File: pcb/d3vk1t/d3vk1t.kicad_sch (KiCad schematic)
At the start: 0 parts

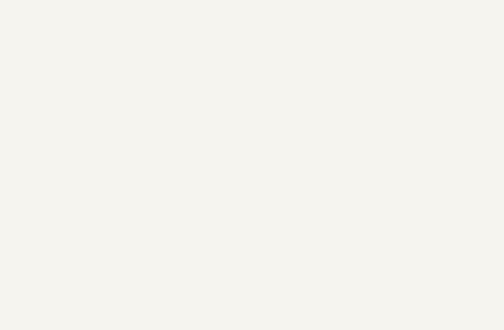
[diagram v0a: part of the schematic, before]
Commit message: [doc: update mcu pinout, pcb: update board shape]
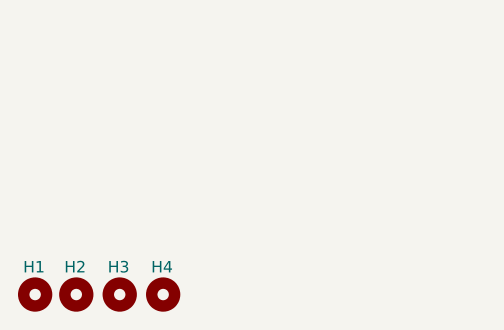
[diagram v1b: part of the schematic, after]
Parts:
- added H1, H2, H3, H4: MountingHole, MountingHole:MountingHole_3.2mm_M3_Pad_Via, symbol Mechanical:MountingHole
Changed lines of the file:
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@@
 (kicad_sch (version 20230121) (generator eeschema)
   (paper "A4")
+  (symbol (lib_id "Mechanical:MountingHole") (at 61.214 178.562 0) (unit 1)
+    (in_bom yes) (on_board yes) (dnp no)
+    (property "Reference" "H4" (at 59.8799 175.5177 0)
+      (effects (font (size 1.27 1.27)) (justify left))
+    )
+    (property "Value" "MountingHole" (at 64.008 180.467 0)
+      (effects (font (size 1.27 1.27)) (justify left) hide)
+    )
+    (property "Footprint" "MountingHole:MountingHole_3.2mm_M3_Pad_Via" (at 61.214 178.562 0)
+      (effects (font (size 1.27 1.27)) hide)
+    )
+    (property "Datasheet" "~" (at 61.214 178.562 0)
+      (effects (font (size 1.27 1.27)) hide)
+    )
+    (instances
+      (project "d3vk1t"
+        (path "/4ea523ae-7c45-478e-a9cc-6f4833d1a9d5"
+          (reference "H4") (unit 1)
+        )
+      )
+    )
+  )
+  (symbol (lib_id "Mechanical:MountingHole") (at 51.562 178.562 0) (unit 1)
+    (in_bom yes) (on_board yes) (dnp no)
+    (property "Reference" "H2" (at 50.2279 175.5177 0)
+      (effects (font (size 1.27 1.27)) (justify left))
+    )
+    (property "Value" "MountingHole" (at 54.356 180.467 0)
+      (effects (font (size 1.27 1.27)) (justify left) hide)
+    )
+    (property "Footprint" "MountingHole:MountingHole_3.2mm_M3_Pad_Via" (at 51.562 178.562 0)
+      (effects (font (size 1.27 1.27)) hide)
+    )
+    (property "Datasheet" "~" (at 51.562 178.562 0)
+      (effects (font (size 1.27 1.27)) hide)
+    )
+    (instances
+      (project "d3vk1t"
+        (path "/4ea523ae-7c45-478e-a9cc-6f4833d1a9d5"
+          (reference "H2") (unit 1)
+        )
+      )
+    )
+  )
+  (symbol (lib_id "Mechanical:MountingHole") (at 56.388 178.562 0) (unit 1)
+    (in_bom yes) (on_board yes) (dnp no)
+    (property "Reference" "H3" (at 55.0539 175.5177 0)
+      (effects (font (size 1.27 1.27)) (justify left))
+    )
+    (property "Value" "MountingHole" (at 59.182 180.467 0)
+      (effects (font (size 1.27 1.27)) (justify left) hide)
+    )
+    (property "Footprint" "MountingHole:MountingHole_3.2mm_M3_Pad_Via" (at 56.388 178.562 0)
+      (effects (font (size 1.27 1.27)) hide)
+    )
+    (property "Datasheet" "~" (at 56.388 178.562 0)
+      (effects (font (size 1.27 1.27)) hide)
+    )
+    (instances
+      (project "d3vk1t"
+        (path "/4ea523ae-7c45-478e-a9cc-6f4833d1a9d5"
+          (reference "H3") (unit 1)
+        )
+      )
+    )
+  )
+  (symbol (lib_id "Mechanical:MountingHole") (at 46.99 178.562 0) (unit 1)
+    (in_bom yes) (on_board yes) (dnp no)
+    (property "Reference" "H1" (at 45.6559 175.5177 0)
+      (effects (font (size 1.27 1.27)) (justify left))
+    )
+    (property "Value" "MountingHole" (at 49.784 180.467 0)
+      (effects (font (size 1.27 1.27)) (justify left) hide)
+    )
+    (property "Footprint" "MountingHole:MountingHole_3.2mm_M3_Pad_Via" (at 46.99 178.562 0)
+      (effects (font (size 1.27 1.27)) hide)
+    )
+    (property "Datasheet" "~" (at 46.99 178.562 0)
+      (effects (font (size 1.27 1.27)) hide)
+    )
+    (instances
+      (project "d3vk1t"
+        (path "/4ea523ae-7c45-478e-a9cc-6f4833d1a9d5"
+          (reference "H1") (unit 1)
+        )
+      )
+    )
+  )
   (sheet (at 85.852 71.882) (size 22.352 13.97) (fields_autoplaced)
     (stroke (width 0.1524) (type solid))

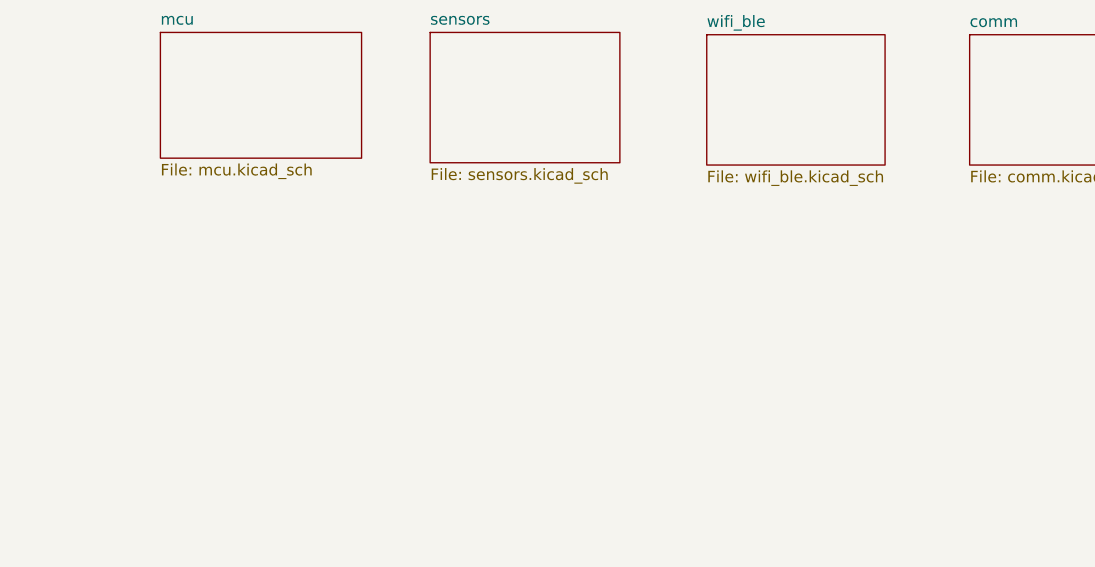
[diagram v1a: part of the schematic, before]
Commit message: doc: added f4 hw dev doc
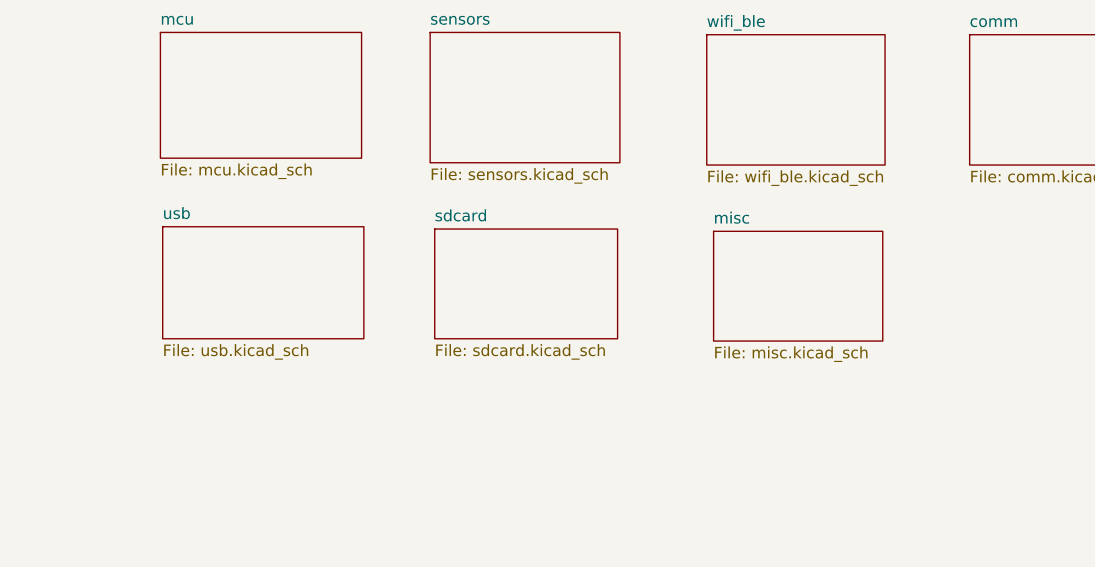
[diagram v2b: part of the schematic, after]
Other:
- added sheet misc (misc.kicad_sch)
- added sheet sdcard (sdcard.kicad_sch)
- added sheet usb (usb.kicad_sch)
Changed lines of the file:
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@@
+    )
+  )
+  (sheet (at 116.332 93.726) (size 20.32 12.192) (fields_autoplaced)
+    (stroke (width 0.1524) (type solid))
+    (fill (color 0 0 0 0.0000))
+    (property "Sheetname" "sdcard" (at 116.332 93.0144 0)
+      (effects (font (size 1.27 1.27)) (justify left bottom))
+    )
+    (property "Sheetfile" "sdcard.kicad_sch" (at 116.332 106.5026 0)
+      (effects (font (size 1.27 1.27)) (justify left top))
+    )
+    (instances
+      (project "d3vk1t"
+        (path "/4ea523ae-7c45-478e-a9cc-6f4833d1a9d5" (page "7"))
+      )
     )
   )
@@
     )
   )
+  (sheet (at 147.32 93.98) (size 18.796 12.192) (fields_autoplaced)
+    (stroke (width 0.1524) (type solid))
+    (fill (color 0 0 0 0.0000))
+    (property "Sheetname" "misc" (at 147.32 93.2684 0)
+      (effects (font (size 1.27 1.27)) (justify left bottom))
+    )
+    (property "Sheetfile" "misc.kicad_sch" (at 147.32 106.7566 0)
+      (effects (font (size 1.27 1.27)) (justify left top))
+    )
+    (instances
+      (project "d3vk1t"
+        (path "/4ea523ae-7c45-478e-a9cc-6f4833d1a9d5" (page "8"))
+      )
+    )
+  )
   (sheet (at 175.768 72.136) (size 22.352 14.478) (fields_autoplaced)
     (stroke (width 0.1524) (type solid))
@@
       )
     )
+  )
+  (sheet (at 86.106 93.472) (size 22.352 12.446) (fields_autoplaced)
+    (stroke (width 0.1524) (type solid))
+    (fill (color 0 0 0 0.0000))
+    (property "Sheetname" "usb" (at 86.106 92.7604 0)
+      (effects (font (size 1.27 1.27)) (justify left bottom))
+    )
+    (property "Sheetfile" "usb.kicad_sch" (at 86.106 106.5026 0)
+      (effects (font (size 1.27 1.27)) (justify left top))
+    )
+    (instances
+      (project "d3vk1t"
+        (path "/4ea523ae-7c45-478e-a9cc-6f4833d1a9d5" (page "6"))
+      )
+    )

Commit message: [update all schematics sheets]
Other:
- added sheet display (display.kicad_sch)
- added sheet memories (memories.kicad_sch)
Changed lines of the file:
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@@
     )
   )
-  (sheet (at 85.852 71.882) (size 22.352 13.97) (fields_autoplaced)
+  (sheet (at 132.08 76.2) (size 20.32 33.02)
     (stroke (width 0.1524) (type solid))
     (fill (color 0 0 0 0.0000))
-    (property "Sheetname" "mcu" (at 85.852 71.1704 0)
+    (property "Sheetname" "mcu" (at 132.08 75.4884 0)
       (effects (font (size 1.27 1.27)) (justify left bottom))
     )
-    (property "Sheetfile" "mcu.kicad_sch" (at 85.852 86.4366 0)
+    (property "Sheetfile" "mcu.kicad_sch" (at 132.08 109.22 0)
       (effects (font (size 1.27 1.27)) (justify left top))
     )
@@
     )
   )
-  (sheet (at 146.558 72.136) (size 19.812 14.478) (fields_autoplaced)
+  (sheet (at 167.64 78.74) (size 20.32 12.7) (fields_autoplaced)
     (stroke (width 0.1524) (type solid))
     (fill (color 0 0 0 0.0000))
-    (property "Sheetname" "wifi_ble" (at 146.558 71.4244 0)
+    (property "Sheetname" "wifi_ble" (at 167.64 78.0284 0)
       (effects (font (size 1.27 1.27)) (justify left bottom))
     )
-    (property "Sheetfile" "wifi_ble.kicad_sch" (at 146.558 87.1986 0)
+    (property "Sheetfile" "wifi_ble.kicad_sch" (at 167.64 92.0246 0)
       (effects (font (size 1.27 1.27)) (justify left top))
     )
@@
     )
   )
-  (sheet (at 116.332 93.726) (size 20.32 12.192) (fields_autoplaced)
+  (sheet (at 167.64 116.84) (size 20.32 12.7) (fields_autoplaced)
     (stroke (width 0.1524) (type solid))
     (fill (color 0 0 0 0.0000))
-    (property "Sheetname" "sdcard" (at 116.332 93.0144 0)
+    (property "Sheetname" "display" (at 167.64 116.1284 0)
       (effects (font (size 1.27 1.27)) (justify left bottom))
     )
-    (property "Sheetfile" "sdcard.kicad_sch" (at 116.332 106.5026 0)
+    (property "Sheetfile" "display.kicad_sch" (at 167.64 130.1246 0)
+      (effects (font (size 1.27 1.27)) (justify left top))
+    )
+    (instances
+      (project "d3vk1t"
+        (path "/4ea523ae-7c45-478e-a9cc-6f4833d1a9d5" (page "9"))
+      )
+    )
+  )
+  (sheet (at 93.98 96.52) (size 20.32 12.7) (fields_autoplaced)
+    (stroke (width 0.1524) (type solid))
+    (fill (color 0 0 0 0.0000))
+    (property "Sheetname" "memories" (at 93.98 95.8084 0)
+      (effects (font (size 1.27 1.27)) (justify left bottom))
+    )
+    (property "Sheetfile" "memories.kicad_sch" (at 93.98 109.8046 0)
+      (effects (font (size 1.27 1.27)) (justify left top))
+    )
+    (instances
+      (project "d3vk1t"
+        (path "/4ea523ae-7c45-478e-a9cc-6f4833d1a9d5" (page "10"))
+      )
+    )
+  )
+  (sheet (at 93.98 116.84) (size 20.32 12.7) (fields_autoplaced)
+    (stroke (width 0.1524) (type solid))
+    (fill (color 0 0 0 0.0000))
+    (property "Sheetname" "sdcard" (at 93.98 116.1284 0)
+      (effects (font (size 1.27 1.27)) (justify left bottom))
+    )
+    (property "Sheetfile" "sdcard.kicad_sch" (at 93.98 129.6166 0)
       (effects (font (size 1.27 1.27)) (justify left top))
     )
@@
     )
   )
-  (sheet (at 115.824 71.882) (size 21.082 14.478) (fields_autoplaced)
+  (sheet (at 93.98 76.2) (size 20.32 12.7)
     (stroke (width 0.1524) (type solid))
     (fill (color 0 0 0 0.0000))
-    (property "Sheetname" "sensors" (at 115.824 71.1704 0)
+    (property "Sheetname" "sensors" (at 93.98 75.4884 0)
       (effects (font (size 1.27 1.27)) (justify left bottom))
     )
-    (property "Sheetfile" "sensors.kicad_sch" (at 115.824 86.9446 0)
+    (property "Sheetfile" "sensors.kicad_sch" (at 93.98 88.9 0)
       (effects (font (size 1.27 1.27)) (justify left top))
     )
@@
     )
   )
-  (sheet (at 147.32 93.98) (size 18.796 12.192) (fields_autoplaced)
+  (sheet (at 167.64 96.52) (size 20.32 12.7) (fields_autoplaced)
     (stroke (width 0.1524) (type solid))
     (fill (color 0 0 0 0.0000))
-    (property "Sheetname" "misc" (at 147.32 93.2684 0)
+    (property "Sheetname" "misc" (at 167.64 95.8084 0)
       (effects (font (size 1.27 1.27)) (justify left bottom))
     )
-    (property "Sheetfile" "misc.kicad_sch" (at 147.32 106.7566 0)
+    (property "Sheetfile" "misc.kicad_sch" (at 167.64 109.8046 0)
       (effects (font (size 1.27 1.27)) (justify left top))
     )
@@
     )
   )
-  (sheet (at 175.768 72.136) (size 22.352 14.478) (fields_autoplaced)
+  (sheet (at 167.64 58.42) (size 20.32 12.7) (fields_autoplaced)
     (stroke (width 0.1524) (type solid))
     (fill (color 0 0 0 0.0000))
-    (property "Sheetname" "comm" (at 175.768 71.4244 0)
+    (property "Sheetname" "comm" (at 167.64 57.7084 0)
       (effects (font (size 1.27 1.27)) (justify left bottom))
     )
-    (property "Sheetfile" "comm.kicad_sch" (at 175.768 87.1986 0)
+    (property "Sheetfile" "comm.kicad_sch" (at 167.64 71.7046 0)
       (effects (font (size 1.27 1.27)) (justify left top))
     )
@@
     )
   )
-  (sheet (at 86.106 93.472) (size 22.352 12.446) (fields_autoplaced)
+  (sheet (at 93.98 58.42) (size 20.32 12.7) (fields_autoplaced)
     (stroke (width 0.1524) (type solid))
     (fill (color 0 0 0 0.0000))
-    (property "Sheetname" "usb" (at 86.106 92.7604 0)
+    (property "Sheetname" "usb" (at 93.98 57.7084 0)
       (effects (font (size 1.27 1.27)) (justify left bottom))
     )
-    (property "Sheetfile" "usb.kicad_sch" (at 86.106 106.5026 0)
+    (property "Sheetfile" "usb.kicad_sch" (at 93.98 71.7046 0)
       (effects (font (size 1.27 1.27)) (justify left top))
     )

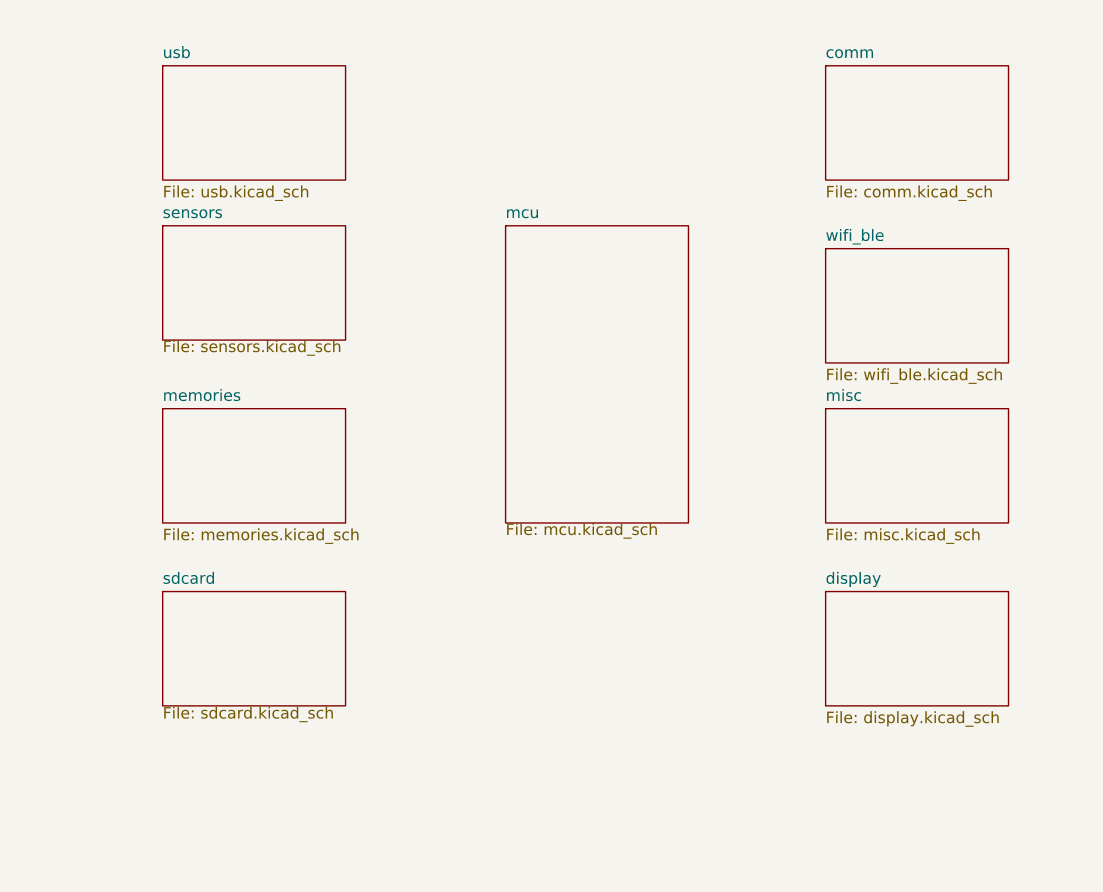
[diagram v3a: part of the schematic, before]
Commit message: sch: update all sch sheets.
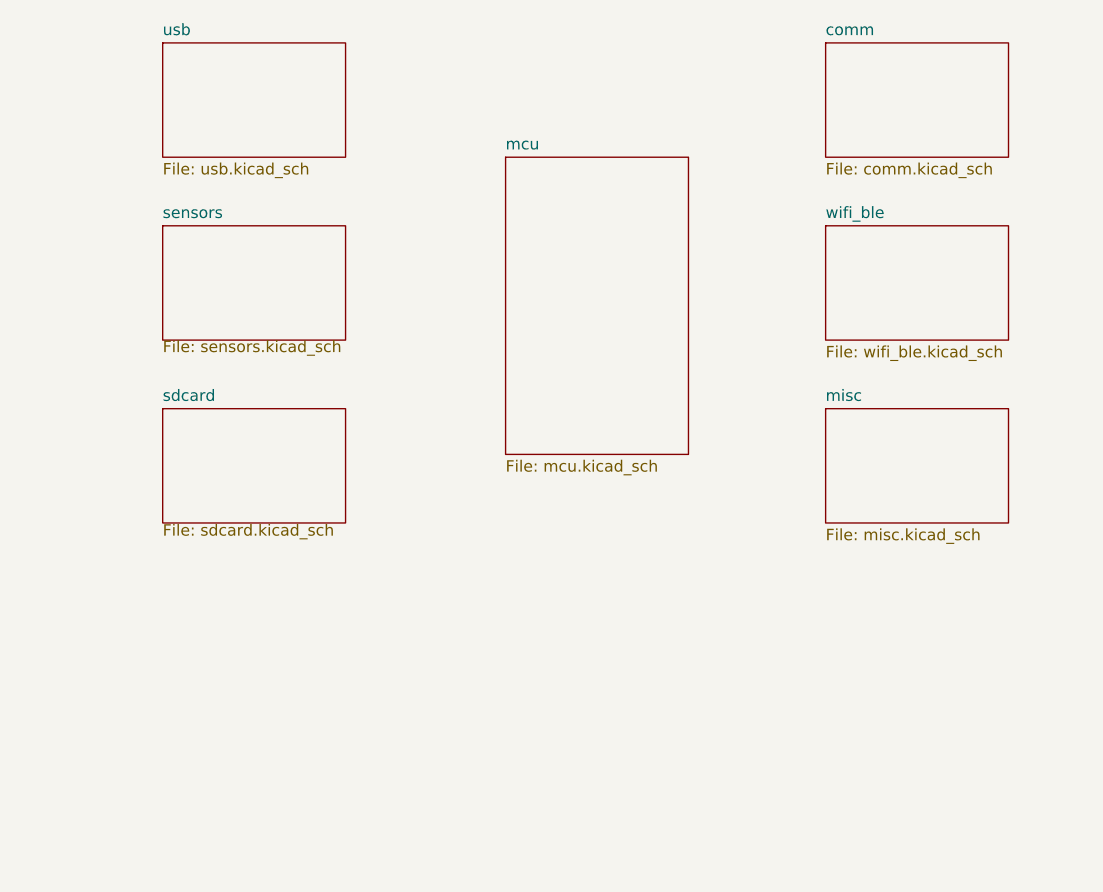
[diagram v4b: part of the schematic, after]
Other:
- removed sheet display
- removed sheet memories
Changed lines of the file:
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@@
     )
   )
-  (sheet (at 132.08 76.2) (size 20.32 33.02)
+  (sheet (at 132.08 68.58) (size 20.32 33.02) (fields_autoplaced)
     (stroke (width 0.1524) (type solid))
     (fill (color 0 0 0 0.0000))
-    (property "Sheetname" "mcu" (at 132.08 75.4884 0)
+    (property "Sheetname" "mcu" (at 132.08 67.8684 0)
       (effects (font (size 1.27 1.27)) (justify left bottom))
     )
-    (property "Sheetfile" "mcu.kicad_sch" (at 132.08 109.22 0)
+    (property "Sheetfile" "mcu.kicad_sch" (at 132.08 102.1846 0)
       (effects (font (size 1.27 1.27)) (justify left top))
     )
@@
     )
   )
-  (sheet (at 167.64 78.74) (size 20.32 12.7) (fields_autoplaced)
+  (sheet (at 167.64 76.2) (size 20.32 12.7) (fields_autoplaced)
     (stroke (width 0.1524) (type solid))
     (fill (color 0 0 0 0.0000))
-    (property "Sheetname" "wifi_ble" (at 167.64 78.0284 0)
+    (property "Sheetname" "wifi_ble" (at 167.64 75.4884 0)
       (effects (font (size 1.27 1.27)) (justify left bottom))
     )
-    (property "Sheetfile" "wifi_ble.kicad_sch" (at 167.64 92.0246 0)
+    (property "Sheetfile" "wifi_ble.kicad_sch" (at 167.64 89.4846 0)
       (effects (font (size 1.27 1.27)) (justify left top))
     )
@@
     )
   )
-  (sheet (at 167.64 116.84) (size 20.32 12.7) (fields_autoplaced)
-    (stroke (width 0.1524) (type solid))
-    (fill (color 0 0 0 0.0000))
-    (property "Sheetname" "display" (at 167.64 116.1284 0)
-      (effects (font (size 1.27 1.27)) (justify left bottom))
-    )
-    (property "Sheetfile" "display.kicad_sch" (at 167.64 130.1246 0)
-      (effects (font (size 1.27 1.27)) (justify left top))
-    )
-    (instances
-      (project "d3vk1t"
-        (path "/4ea523ae-7c45-478e-a9cc-6f4833d1a9d5" (page "9"))
-      )
-    )
-  )
   (sheet (at 93.98 96.52) (size 20.32 12.7) (fields_autoplaced)
     (stroke (width 0.1524) (type solid))
     (fill (color 0 0 0 0.0000))
-    (property "Sheetname" "memories" (at 93.98 95.8084 0)
+    (property "Sheetname" "sdcard" (at 93.98 95.8084 0)
       (effects (font (size 1.27 1.27)) (justify left bottom))
     )
-    (property "Sheetfile" "memories.kicad_sch" (at 93.98 109.8046 0)
-      (effects (font (size 1.27 1.27)) (justify left top))
-    )
-    (instances
-      (project "d3vk1t"
-        (path "/4ea523ae-7c45-478e-a9cc-6f4833d1a9d5" (page "10"))
-      )
-    )
-  )
-  (sheet (at 93.98 116.84) (size 20.32 12.7) (fields_autoplaced)
-    (stroke (width 0.1524) (type solid))
-    (fill (color 0 0 0 0.0000))
-    (property "Sheetname" "sdcard" (at 93.98 116.1284 0)
-      (effects (font (size 1.27 1.27)) (justify left bottom))
-    )
-    (property "Sheetfile" "sdcard.kicad_sch" (at 93.98 129.6166 0)
+    (property "Sheetfile" "sdcard.kicad_sch" (at 93.98 109.2966 0)
       (effects (font (size 1.27 1.27)) (justify left top))
     )
@@
     )
   )
-  (sheet (at 167.64 58.42) (size 20.32 12.7) (fields_autoplaced)
+  (sheet (at 167.64 55.88) (size 20.32 12.7) (fields_autoplaced)
     (stroke (width 0.1524) (type solid))
     (fill (color 0 0 0 0.0000))
-    (property "Sheetname" "comm" (at 167.64 57.7084 0)
+    (property "Sheetname" "comm" (at 167.64 55.1684 0)
       (effects (font (size 1.27 1.27)) (justify left bottom))
     )
-    (property "Sheetfile" "comm.kicad_sch" (at 167.64 71.7046 0)
+    (property "Sheetfile" "comm.kicad_sch" (at 167.64 69.1646 0)
       (effects (font (size 1.27 1.27)) (justify left top))
     )
@@
     )
   )
-  (sheet (at 93.98 58.42) (size 20.32 12.7) (fields_autoplaced)
+  (sheet (at 93.98 55.88) (size 20.32 12.7) (fields_autoplaced)
     (stroke (width 0.1524) (type solid))
     (fill (color 0 0 0 0.0000))
-    (property "Sheetname" "usb" (at 93.98 57.7084 0)
+    (property "Sheetname" "usb" (at 93.98 55.1684 0)
       (effects (font (size 1.27 1.27)) (justify left bottom))
     )
-    (property "Sheetfile" "usb.kicad_sch" (at 93.98 71.7046 0)
+    (property "Sheetfile" "usb.kicad_sch" (at 93.98 69.1646 0)
       (effects (font (size 1.27 1.27)) (justify left top))
     )
